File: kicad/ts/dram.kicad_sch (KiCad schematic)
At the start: 10 parts, among them M0 MMN4164, M1 MMN4164, M2 MMN4164, M3 MMN4164, M4 MMN4164, M5 MMN4164, M6 MMN4164, M7 MMN4164

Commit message: update footprints
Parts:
- L1: footprint (none) -> Package_DIP:DIP-20_W7.62mm
- M0, M1, M2, M3, M4, M5, M6, M7: footprint Cobra_original:DIP-16_W7.62mm -> Package_DIP:DIP-16_W7.62mm
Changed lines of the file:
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@@
 			)
 		)
-		(property "Footprint" "Cobra_original:DIP-16_W7.62mm"
+		(property "Footprint" "Package_DIP:DIP-16_W7.62mm"
 			(at 125.73 59.055 0)
 			(effects
@@
 			)
 		)
-		(property "Footprint" "Cobra_original:DIP-16_W7.62mm"
+		(property "Footprint" "Package_DIP:DIP-16_W7.62mm"
 			(at 48.26 127.635 0)
 			(effects
@@
 			)
 		)
-		(property "Footprint" "Cobra_original:DIP-16_W7.62mm"
+		(property "Footprint" "Package_DIP:DIP-16_W7.62mm"
 			(at 164.465 59.055 0)
 			(effects
@@
 			)
 		)
-		(property "Footprint" "Cobra_original:DIP-16_W7.62mm"
+		(property "Footprint" "Package_DIP:DIP-16_W7.62mm"
 			(at 164.465 127.635 0)
 			(effects
@@
 			)
 		)
-		(property "Footprint" "Cobra_original:DIP-16_W7.62mm"
+		(property "Footprint" "Package_DIP:DIP-16_W7.62mm"
 			(at 86.995 127.635 0)
 			(effects
@@
 			)
 		)
-		(property "Footprint" "Cobra_original:DIP-16_W7.62mm"
+		(property "Footprint" "Package_DIP:DIP-16_W7.62mm"
 			(at 125.73 127.635 0)
 			(effects
@@
 			)
 		)
-		(property "Footprint" ""
+		(property "Footprint" "Package_DIP:DIP-20_W7.62mm"
 			(at 101.6 209.55 0)
 			(effects
@@
 			)
 		)
-		(property "Footprint" "Cobra_original:DIP-16_W7.62mm"
+		(property "Footprint" "Package_DIP:DIP-16_W7.62mm"
 			(at 86.995 59.055 0)
 			(effects
@@
 			)
 		)
-		(property "Footprint" "Cobra_original:DIP-16_W7.62mm"
+		(property "Footprint" "Package_DIP:DIP-16_W7.62mm"
 			(at 48.26 59.055 0)
 			(effects

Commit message: Schemativ corrections, work started on pcb
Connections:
- net D0: now also M0.2 (D); no longer M0.14 (Q)
- net D1: now also M1.2 (D); no longer M1.14 (Q)
- net D2: now also M2.2 (D); no longer M2.14 (Q)
- net D3: now also M3.2 (D); no longer M3.14 (Q)
- net D4: now also M4.2 (D); no longer M4.14 (Q)
- net D5: now also M5.2 (D); no longer M5.14 (Q)
- net D6: now also M6.2 (D); no longer M6.14 (Q)
- net D7: now also M7.2 (D); no longer M7.14 (Q)
- net MD0: now also M0.14 (Q); no longer M0.2 (D)
- net MD1: now also M1.14 (Q); no longer M1.2 (D)
- net MD2: now also M2.14 (Q); no longer M2.2 (D)
- net MD3: now also M3.14 (Q); no longer M3.2 (D)
- net MD4: now also M4.14 (Q); no longer M4.2 (D)
- net MD5: now also M5.14 (Q); no longer M5.2 (D)
- net MD6: now also M6.14 (Q); no longer M6.2 (D)
- net MD7: now also M7.14 (Q); no longer M7.2 (D)
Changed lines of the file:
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@@
 	)
 	(label "MD5"
-		(at 103.505 107.315 180)
+		(at 103.505 104.775 180)
 		(fields_autoplaced yes)
 		(effects
@@
 	)
 	(label "MD4"
-		(at 64.77 107.315 180)
+		(at 64.77 104.775 180)
 		(fields_autoplaced yes)
 		(effects
@@
 	)
 	(label "MD6"
-		(at 142.24 107.315 180)
+		(at 142.24 104.775 180)
 		(fields_autoplaced yes)
 		(effects
@@
 	)
 	(label "D0"
-		(at 64.77 36.195 180)
+		(at 64.77 38.735 180)
 		(fields_autoplaced yes)
 		(effects
@@
 	)
 	(label "D7"
-		(at 180.975 104.775 180)
+		(at 180.975 107.315 180)
 		(fields_autoplaced yes)
 		(effects
@@
 	)
 	(label "MD7"
-		(at 180.975 107.315 180)
+		(at 180.975 104.775 180)
 		(fields_autoplaced yes)
 		(effects
@@
 	)
 	(label "D5"
-		(at 103.505 104.775 180)
+		(at 103.505 107.315 180)
 		(fields_autoplaced yes)
 		(effects
@@
 	)
 	(label "MD2"
-		(at 142.24 38.735 180)
+		(at 142.24 36.195 180)
 		(fields_autoplaced yes)
 		(effects
@@
 	)
 	(label "D1"
-		(at 103.505 36.195 180)
+		(at 103.505 38.735 180)
 		(fields_autoplaced yes)
 		(effects
@@
 	)
 	(label "MD0"
-		(at 64.77 38.735 180)
+		(at 64.77 36.195 180)
 		(fields_autoplaced yes)
 		(effects
@@
 	)
 	(label "MD1"
-		(at 103.505 38.735 180)
+		(at 103.505 36.195 180)
 		(fields_autoplaced yes)
 		(effects
@@
 	)
 	(label "D2"
-		(at 142.24 36.195 180)
+		(at 142.24 38.735 180)
 		(fields_autoplaced yes)
 		(effects
@@
 	)
 	(label "MD3"
-		(at 180.975 38.735 180)
+		(at 180.975 36.195 180)
 		(fields_autoplaced yes)
 		(effects
@@
 	)
 	(label "D4"
-		(at 64.77 104.775 180)
+		(at 64.77 107.315 180)
 		(fields_autoplaced yes)
 		(effects
@@
 	)
 	(label "D6"
-		(at 142.24 104.775 180)
+		(at 142.24 107.315 180)
 		(fields_autoplaced yes)
 		(effects
@@
 	)
 	(label "D3"
-		(at 180.975 36.195 180)
-		(fields_autoplaced yes)
-		(effects
+		(at 180.975 38.735 180)
+		(fields_autoplaced yes)
+		(effects

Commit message: 4164 footprint corrected, more pcb traces
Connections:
- net XA1: now also M0.7 (A1), M1.7 (A1), M2.7 (A1), M3.7 (A1), M4.7 (A1), M5.7 (A1), M6.7 (A1), M7.7 (A1); no longer M0.6 (A1), M1.6 (A1), M2.6 (A1), M3.6 (A1), M4.6 (A1), M5.6 (A1), M6.6 (A1), M7.6 (A1)
- net XA2: now also M0.6 (A2), M1.6 (A2), M2.6 (A2), M3.6 (A2), M4.6 (A2), M5.6 (A2), M6.6 (A2), M7.6 (A2); no longer M0.7 (A2), M1.7 (A2), M2.7 (A2), M3.7 (A2), M4.7 (A2), M5.7 (A2), M6.7 (A2), M7.7 (A2)

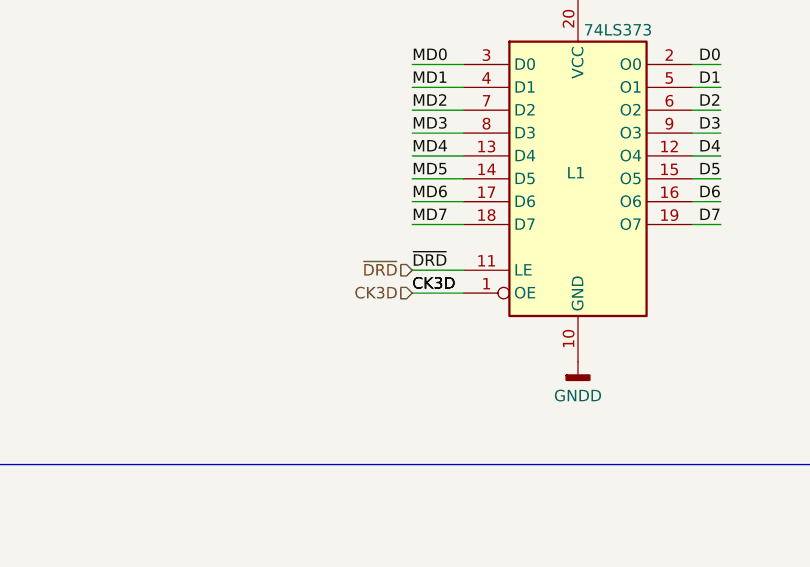
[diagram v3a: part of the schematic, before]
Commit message: Schematic corrections, all pcb traces placed, todo footprints check
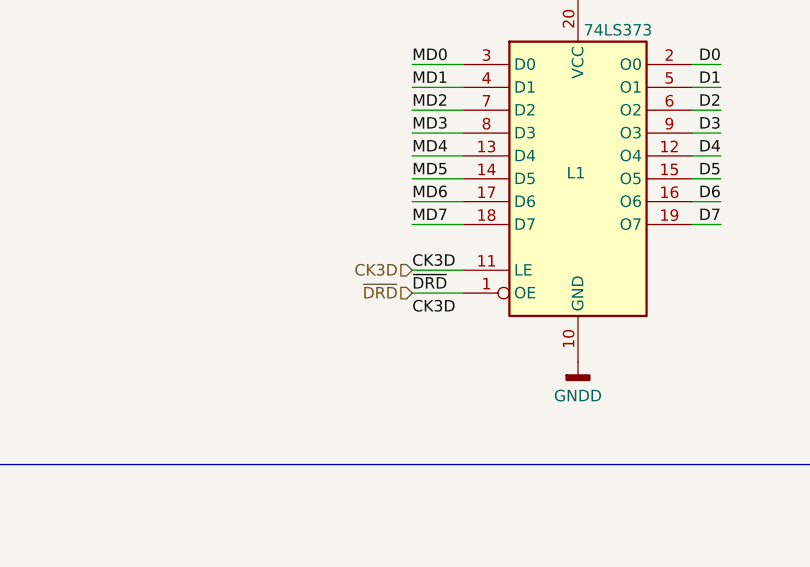
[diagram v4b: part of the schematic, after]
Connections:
- net CK3D: now also L1.11 (LE); no longer L1.1 (OE)
- net ~{DRD}: now also L1.1 (OE); no longer L1.11 (LE)
